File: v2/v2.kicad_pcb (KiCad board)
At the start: 2 copper layers, 10.3 x 7.2 mm, 105 parts, among them J1 Conn_01x04_Pin, J2 Conn_01x04_Pin, J3 Conn_01x04_Pin, SW1 SW_Push, SW10 SW_Push, SW11 SW_Push, SW12 SW_Push, SW13 SW_Push, SW14 SW_Push, SW15 SW_Push, SW16 SW_Push, SW17 SW_Push, SW18 SW_Push, SW19 SW_Push, SW2 SW_Push, SW20 SW_Push, SW21 SW_Push, SW22 SW_Push, SW23 SW_Push, SW24 SW_Push, SW25 SW_Push, SW26 SW_Push, SW27 SW_Push, SW28 SW_Push, SW29 SW_Push, SW3 SW_Push, SW30 SW_Push, SW31 SW_Push, SW32 SW_Push, SW33 RotaryEncoder_Switch, SW4 SW_Push, SW5 SW_Push, SW6 SW_Push, SW7 SW_Push, SW8 SW_Push, SW9 SW_Push, U1 Pico, U2 Pico

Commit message: finished layout for all components
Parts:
- J1, U2: moved to B.Cu
- moved SW28 278.8 mm to (259.3, 207.9), turned to -31 degrees
- moved SW21 257.3 mm to (239.6, 198.9), turned to -21 degrees
- moved J3 237.1 mm to (281.9, 159.5), turned to -75.5 degrees
- moved D28 233.9 mm to (249.4, 207.9), turned to -121 degrees
- moved D6 227.0 mm to (227.8, 99.5), turned to -90 degrees
- moved SW20 221.9 mm to (235.8, 133.5), turned to -1 degrees
- moved D21 220.4 mm to (229.7, 200.7), turned to -111 degrees
- moved D33 218.1 mm to (247.3, 179.2), turned to -96 degrees
- moved SW33 216.4 mm to (257.3, 173.9), turned to 174 degrees
- moved R3 213.0 mm to (273.6, 140.1), turned to 89.5 degrees
- moved J1 212.4 mm to (257.1, 149.8), turned to 88.5 degrees
- moved J2 212.3 mm to (261.6, 149.9), turned to 89 degrees
- moved D14 212.2 mm to (209.0, 197.5), turned to -101 degrees
- moved R4 212.2 mm to (273.8, 127.8), turned to 89.5 degrees
- moved D13 211.5 mm to (227.5, 118.9), turned to -91 degrees
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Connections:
- D1 pad 1: Row 1 -> Row 2
- D15 pad 1: Row 3 -> Row 4
- D2 pad 1: Row 1 -> Net-(D2-K)
- D22 pad 1: Row 4 -> Row 5
- D3 pad 1: Row 1 -> Net-(D2-K)
- D4 pad 1: Row 1 -> Net-(D2-K)
- D5 pad 1: Row 1 -> Net-(D2-K)
- D6 pad 1: Row 1 -> Net-(D2-K)
- D7 pad 1: Row 1 -> Net-(D2-K)
- D8 pad 1: Row 2 -> Row 3
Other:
- board size 10.3 x 7.2 mm -> 9.7 x 8.4 mm

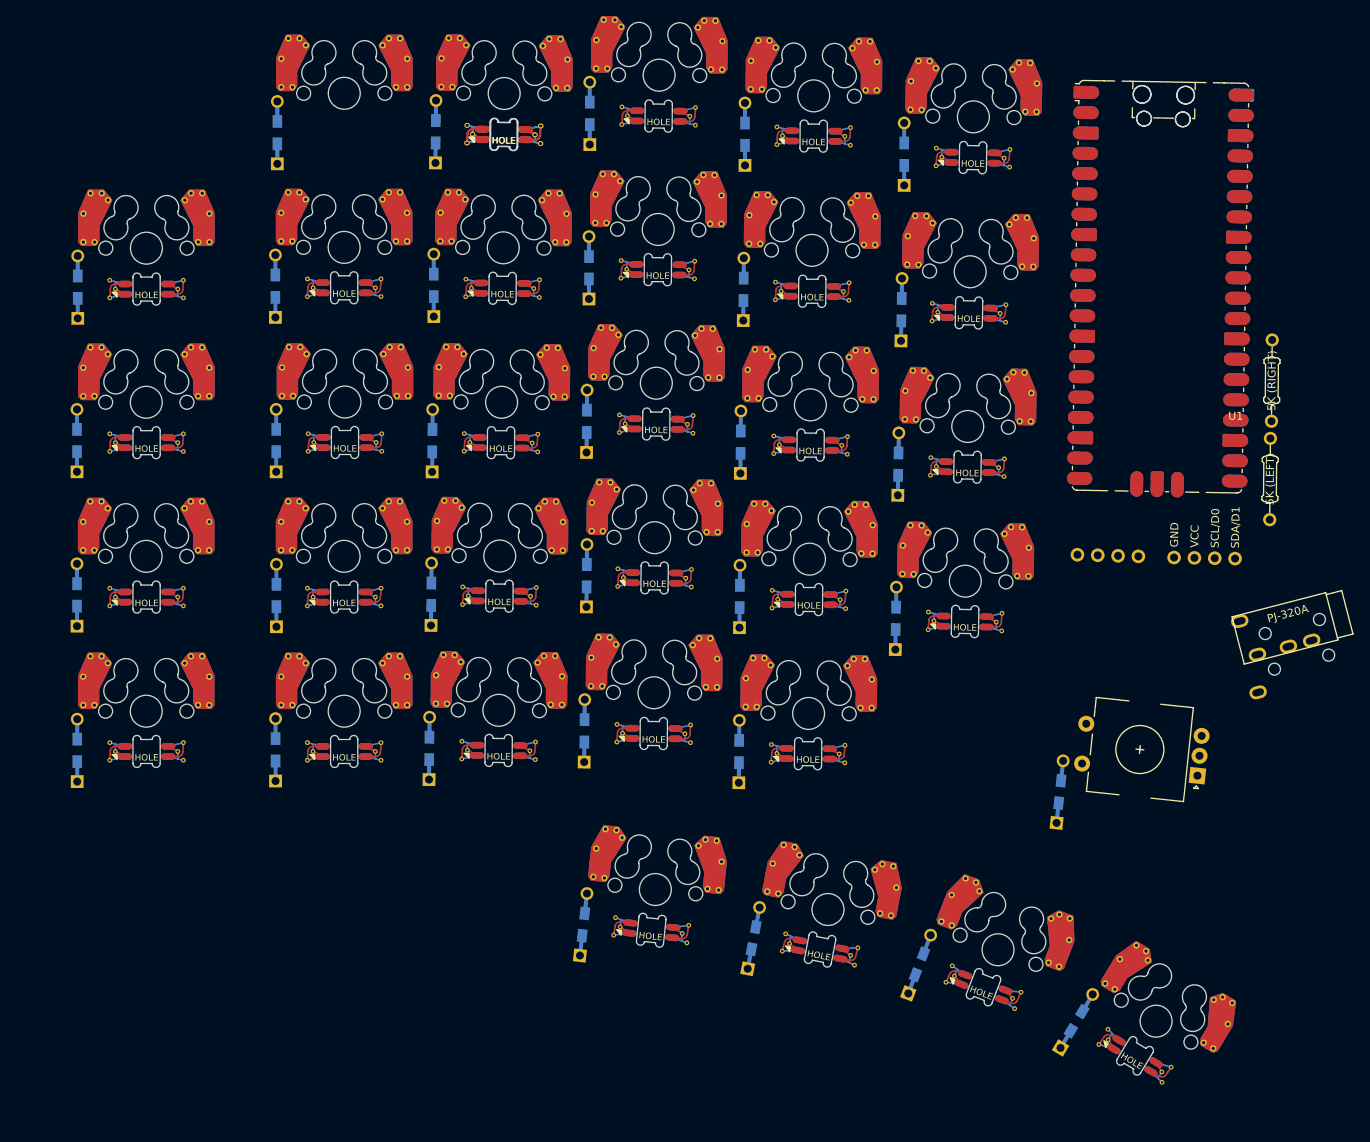
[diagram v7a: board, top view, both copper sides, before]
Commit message: added custom dual side hybrid diode footprint
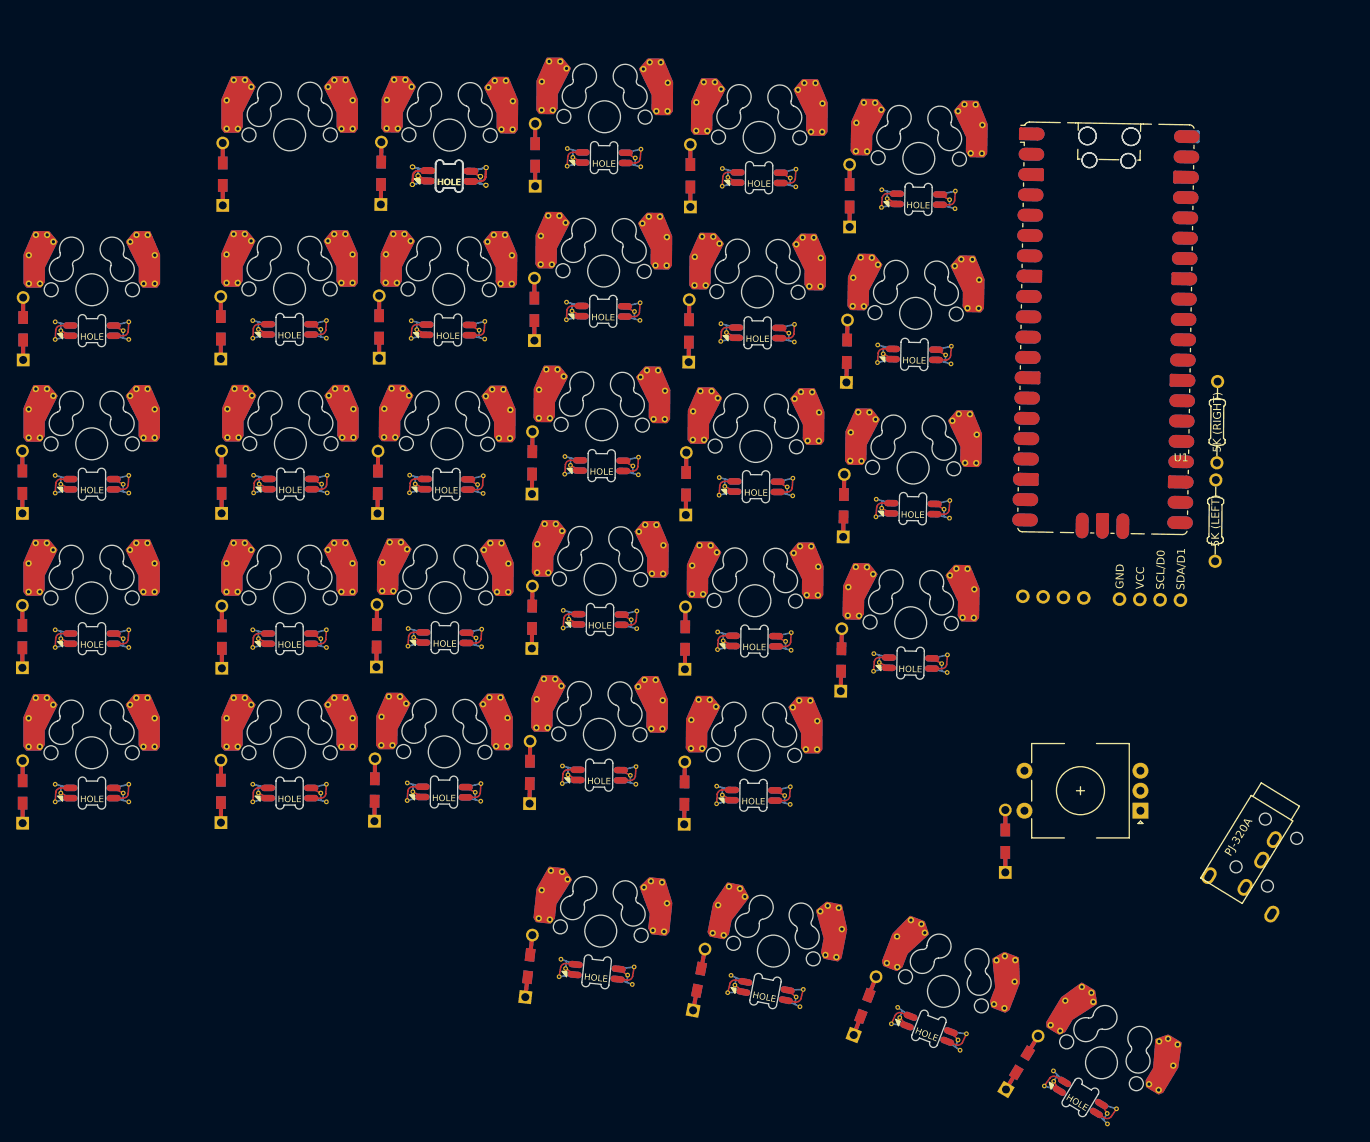
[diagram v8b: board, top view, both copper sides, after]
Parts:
- D1, D10, D11, D12, D13, D14, D15, D16, D17, D18, D19, D2, D20, D21, D22, D23, D24, D25, D26, D27, D28, D29, D3, D30, D31, D32, D33, D4, D5, D6, D7, D8, D9: footprint Keebio-Parts:Diode-Hybrid-Back -> Keebio-Parts:Diode-Hybrid-Dual
- moved J3 23.8 mm to (275.8, 182.4), turned to -31.5 degrees
- moved D33 9.19 mm to (240.5, 185.4), turned to -90 degrees
- moved SW33 9.04 mm to (249.9, 179.1), turned to 180 degrees
- moved D3 8.58 mm to (162.5, 101.9)
- moved J1 8.58 mm to (250.3, 154.9)
- moved LED14 8.58 mm to (211.5, 199.1)
- moved LED17 8.58 mm to (170.7, 135.7)
- moved LED26 8.58 mm to (209.2, 155.3)
- moved R3 8.58 mm to (266.7, 145.3)
- moved SW2 8.58 mm to (151.0, 97.1)
- moved SW27 8.58 mm to (228.6, 158.1)
- moved SW29 8.58 mm to (151.0, 174.3)
- moved D1 8.58 mm to (117.7, 121.3)
- moved LED1 8.58 mm to (126.3, 116.5)
- moved LED15 8.58 mm to (126.3, 155.0)
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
